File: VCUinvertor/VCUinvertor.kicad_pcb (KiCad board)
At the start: 2 copper layers, 97.3 x 113.8 mm, 97 parts, among them J7 PowerSupply, J8 CAN_NXP, J9 BACKLIGHT, Q1 2N7002, Q10 2N7002, Q2 2N7002, Q3 2N7002, Q4 2N7002, Q5 2N7002, Q6 2N7002, Q7 2N7002, Q8 2N7002, Q9 2N7002, U1 TJA1448ATK, U2 REF3433T, U3 TLV76150DCY

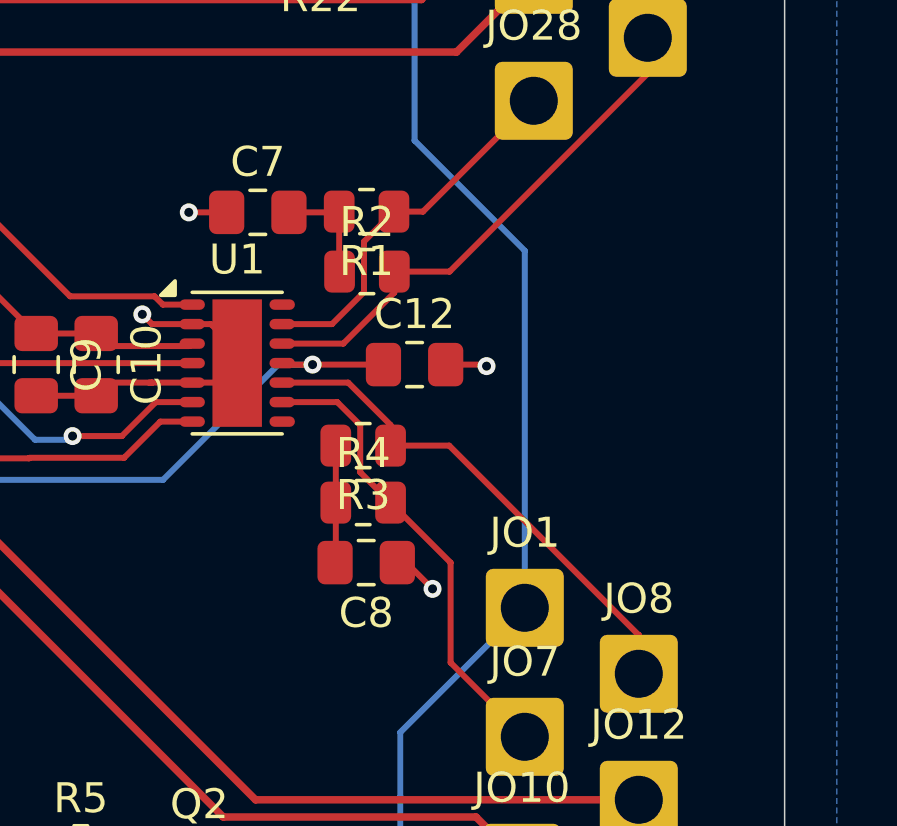
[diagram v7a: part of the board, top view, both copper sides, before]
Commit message: Added datasheets for MOS
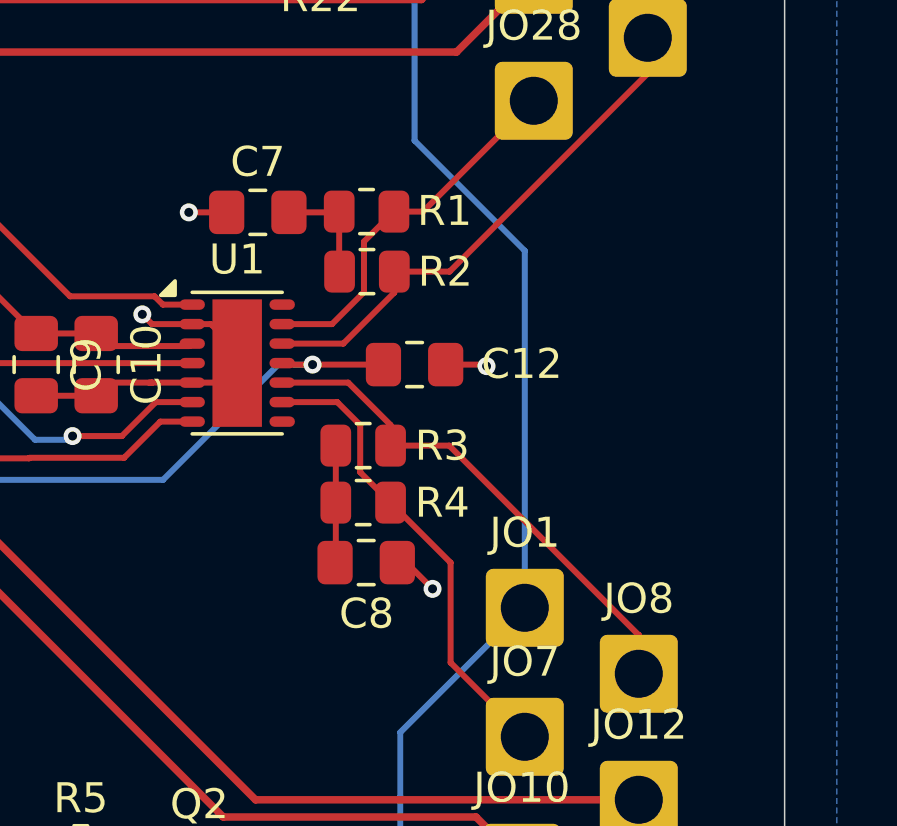
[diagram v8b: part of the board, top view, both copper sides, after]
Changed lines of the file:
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@@
 		(tags "resistor")
 		(property "Reference" "R1"
-			(at 0 -1.65 0)
+			(at -2.6 0.01875 0)
 			(layer "F.SilkS")
 			(effects
@@
 		(tags "resistor")
 		(property "Reference" "R4"
-			(at 0 -1.65 0)
+			(at 2.6375 0.00625 0)
 			(layer "F.SilkS")
 			(effects
@@
 		(tags "resistor")
 		(property "Reference" "R3"
-			(at 0 -1.65 0)
+			(at -2.6375 -0.00625 0)
 			(layer "F.SilkS")
 			(effects
@@
 		(tags "capacitor handsolder")
 		(property "Reference" "C8"
-			(at 0 -1.679999 0)
+			(at -0.0125 -1.70625 0)
 			(layer "F.SilkS")
 			(effects
@@
 		(tags "resistor")
 		(property "Reference" "R2"
-			(at 0 -1.65 0)
+			(at 2.6125 0.00625 0)
 			(layer "F.SilkS")
 			(effects
@@
 		(tags "capacitor handsolder")
 		(property "Reference" "C12"
-			(at 0 -1.679999 0)
+			(at 3.575 -0.01875 0)
 			(layer "F.SilkS")
 			(effects
@@
 		)
 	)
-	(group ""
-		(members "05714dac-fe17-4f57-afc7-cbd955bd4eef" "15ebd7ba-7773-4c3f-87ea-a59f299dbfc9"
-			"35fd12bc-d368-4af9-aad7-c42eb65bef47" "48d89460-0281-4b59-96f0-63c7b3e4913f"
-			"72869a3f-5d90-45a0-b155-07b085738c89" "7de15117-ea6f-44fa-8bab-dbffd5a6e696"
-			"8cd5ae5e-cd70-4728-9ca6-460299b50a7a" "99c211c5-e1b8-486d-9149-ca7a9a99c401"
-			"a83f5756-9649-465e-84b7-aa04add7e8f1"
-		)
-	)
